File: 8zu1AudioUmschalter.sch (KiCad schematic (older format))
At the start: 39 parts, among them IC1 ATMEGA8A-A, IC2 MAX9890, J1 USB, J2 LUM 1503-07, J3 LUM 1503-07, J4 LUM 1503-07, J5 LUM 1503-07, J6 LUM 1503-07, J7 LUM 1503-07, J8 LUM 1503-07, J9 LUM 1503-07, K1 RELAY_2RT, K2 RELAY_2RT, K3 RELAY_2RT, K4 RELAY_2RT, K5 RELAY_2RT, K6 RELAY_2RT, K7 RELAY_2RT, U1 FT232RL, U2 ULN2003, Y1 16Mhz

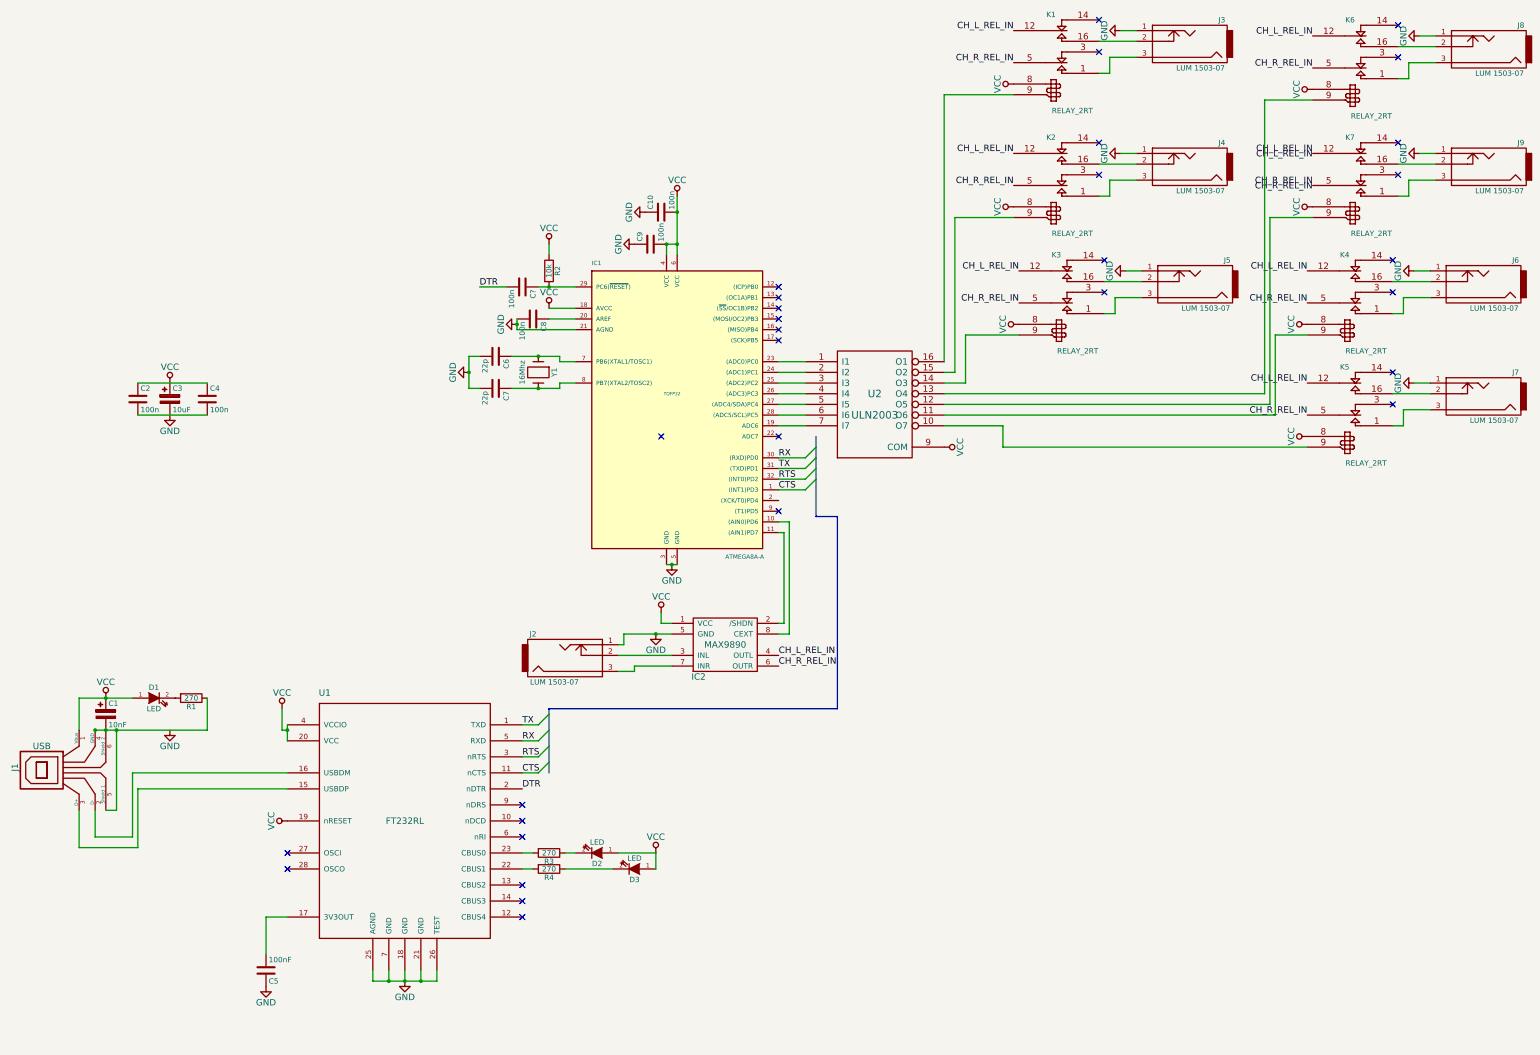
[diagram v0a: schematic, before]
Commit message: Kleinere Anpassungen am MAX9890
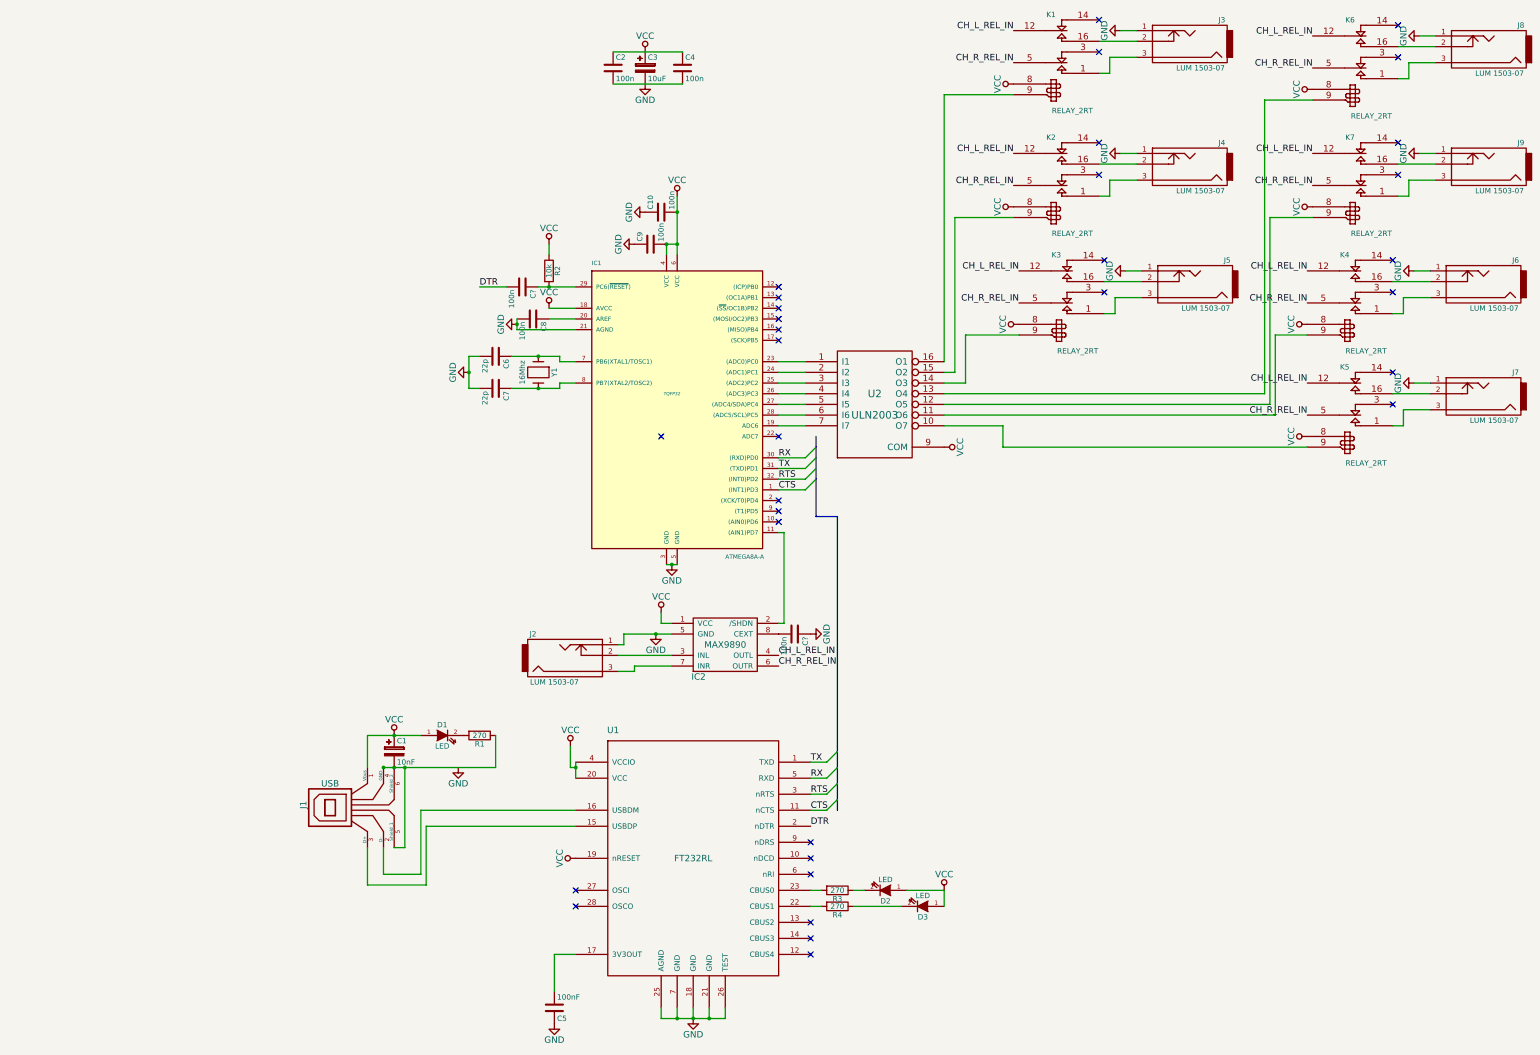
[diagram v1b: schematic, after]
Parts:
- added C?: 100n, symbol C
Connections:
- net GND: now also C?.1
- net at IC1.10 ((AIN0)PD6): no longer IC2.8 (CEXT)
- new net: C?.2, IC2.8 (CEXT)
- no-connect marks 31 -> 33
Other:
- moved on the sheet: C1, C2, C3, C4, C5, D1, D2, D3, J1, R1, R3, R4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

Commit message: Hinzufügen von Status LEDs für die einzelnen Relais
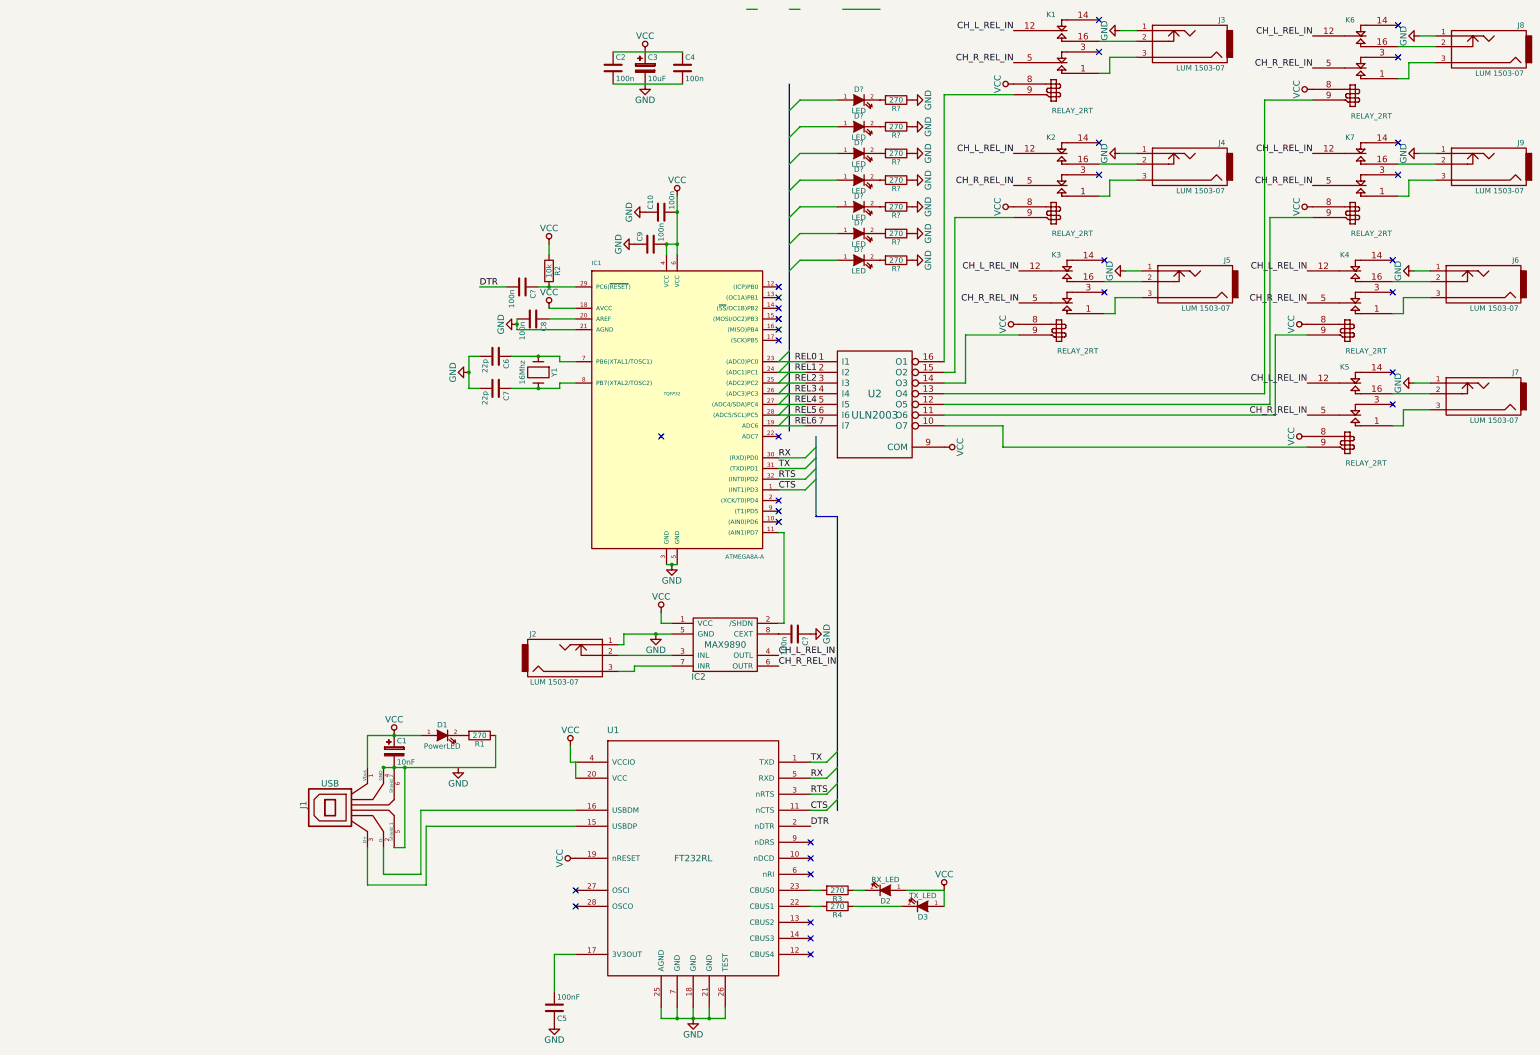
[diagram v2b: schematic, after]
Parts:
- added D? (x7): LED, symbol LED
- added R? (x7): 270, symbol R
- D1: value LED -> PowerLED
- D2: value LED -> RX_LED
- D3: value LED -> TX_LED
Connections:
- net labels added: REL0, REL1, REL2, REL3, REL4, REL5, REL6
- wire segments 151 -> 145

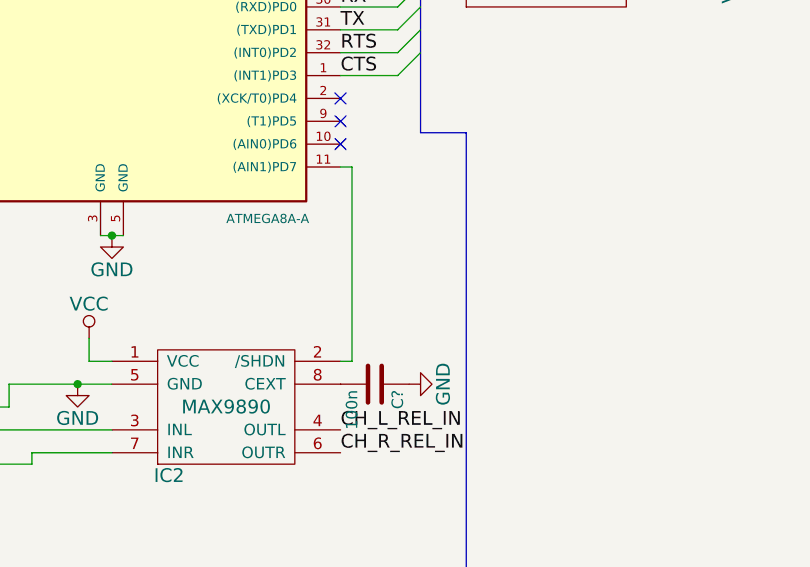
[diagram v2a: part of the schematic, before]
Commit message: Pull Down am MAX9890 um Signal bewusst zu kontrollieren
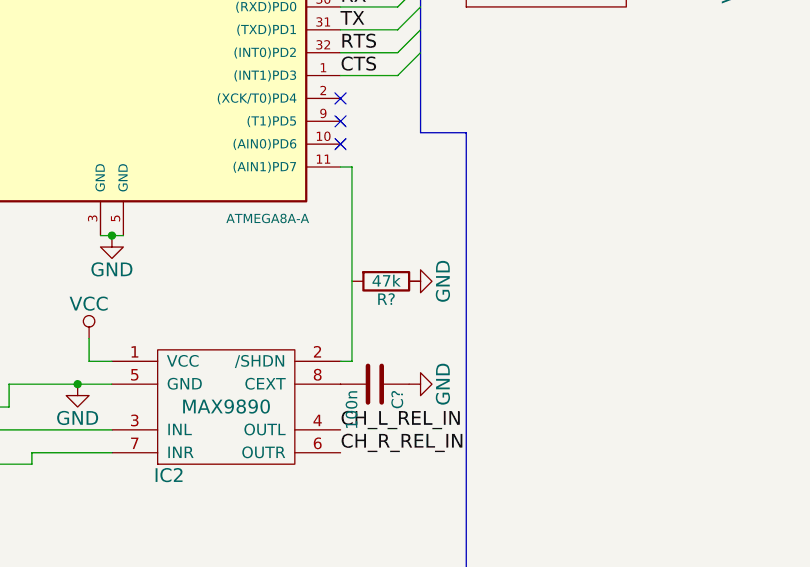
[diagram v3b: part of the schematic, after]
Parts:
- added R?: 47k, symbol R
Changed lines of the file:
@@
 Entry Wire Line
 	8350 3450 8450 3350
+$Comp
+L R R?
+U 1 1 5506D344
+P 8450 6400
+F 0 "R?" V 8530 6400 50  0000 C CNN
+F 1 "47k" V 8450 6400 50  0000 C CNN
+F 2 "" V 8380 6400 30  0000 C CNN
+F 3 "" H 8450 6400 30  0000 C CNN
+	1    8450 6400
+	0    1    1    0
+$EndComp
+$Comp
+L GND #PWR?
+U 1 1 5506D5D9
+P 8550 6400
+F 0 "#PWR?" H 8550 6150 60  0001 C CNN
+F 1 "GND" H 8550 6250 60  0000 C CNN
+F 2 "" H 8550 6400 60  0000 C CNN
+F 3 "" H 8550 6400 60  0000 C CNN
+	1    8550 6400
+	0    -1   -1   0
+$EndComp
 $EndSCHEMATC

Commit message: Hinzufügen der Libs
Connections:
- wire segments 145 -> 142
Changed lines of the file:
@@
 	0    1    1    0
 $EndComp
-Wire Wire Line
-	8350 1000 8450 1000
-Wire Wire Line
-	8050 1000 7950 1000
-Wire Wire Line
-	8850 1000 9200 1000
 $Comp
 L GND #PWR?

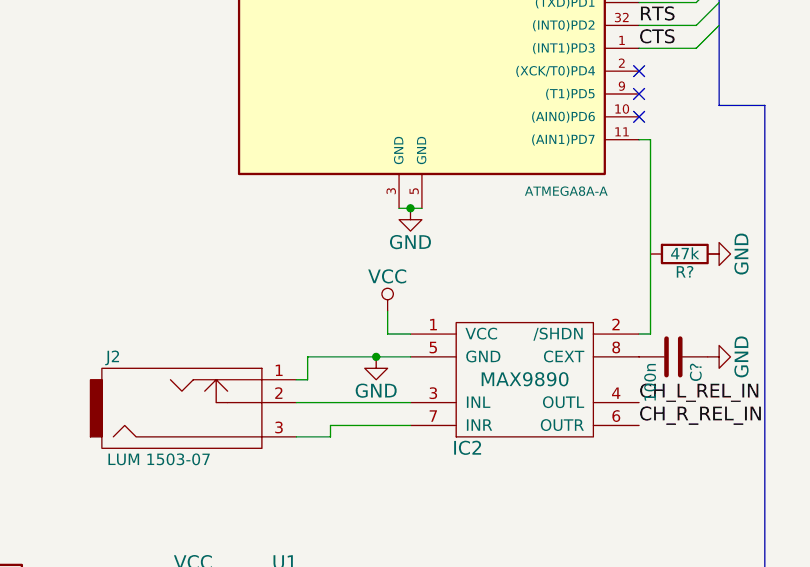
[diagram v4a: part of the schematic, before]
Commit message: Hinzufügen eines VCC stab. Kond. am MAX9890
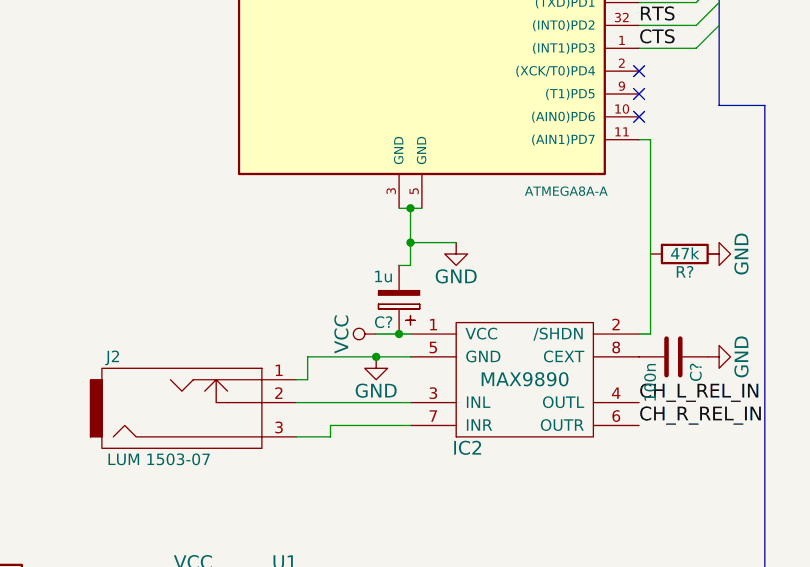
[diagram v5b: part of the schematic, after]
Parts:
- added C?: 1u, symbol CP
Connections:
- net GND: now also C?.2
- net VCC: now also C?.1
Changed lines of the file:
@@
 L GND #PWR017
 U 1 1 5504FEE4
-P 7250 6200
-F 0 "#PWR017" H 7250 5950 60  0001 C CNN
-F 1 "GND" H 7250 6050 60  0000 C CNN
-F 2 "" H 7250 6200 60  0000 C CNN
-F 3 "" H 7250 6200 60  0000 C CNN
-	1    7250 6200
+P 7450 6350
+F 0 "#PWR017" H 7450 6100 60  0001 C CNN
+F 1 "GND" H 7450 6200 60  0000 C CNN
+F 2 "" H 7450 6350 60  0000 C CNN
+F 3 "" H 7450 6350 60  0000 C CNN
+	1    7450 6350
 	1    0    0    -1
 $EndComp
@@
 Connection ~ 5350 4400
 Wire Wire Line
-	7250 6750 7150 6750
-Wire Wire Line
-	7150 6750 7150 6650
-Wire Wire Line
 	6800 6850 7250 6850
 $Comp
@@
 L VCC #PWR020
 U 1 1 55052107
-P 7150 6650
-F 0 "#PWR020" H 7150 6500 60  0001 C CNN
-F 1 "VCC" H 7150 6800 60  0000 C CNN
-F 2 "" H 7150 6650 60  0000 C CNN
-F 3 "" H 7150 6650 60  0000 C CNN
-	1    7150 6650
-	1    0    0    -1
+P 7100 6750
+F 0 "#PWR020" H 7100 6600 60  0001 C CNN
+F 1 "VCC" H 7100 6900 60  0000 C CNN
+F 2 "" H 7100 6750 60  0000 C CNN
+F 3 "" H 7100 6750 60  0000 C CNN
+	1    7100 6750
+	0    -1   -1   0
 $EndComp
 $Comp
@@
 	0    -1   -1   0
 $EndComp
+$Comp
+L CP C?
+U 1 1 5506F49A
+P 7200 6600
+F 0 "C?" H 7225 6700 50  0000 L CNN
+F 1 "1u" H 7225 6500 50  0000 L CNN
+F 2 "" H 7238 6450 30  0000 C CNN
+F 3 "" H 7200 6600 60  0000 C CNN
+	1    7200 6600
+	-1   0    0    1
+$EndComp
+Wire Wire Line
+	7100 6750 7250 6750
+Connection ~ 7200 6750
+Wire Wire Line
+	7200 6450 7250 6450
+Wire Wire Line
+	7250 6450 7250 6200
+Wire Wire Line
+	7450 6350 7250 6350
+Connection ~ 7250 6350
 $EndSCHEMATC

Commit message: Kleinere Anpassungen
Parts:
- removed C1: 10nF, symbol CP
- removed C3: 10uF, symbol CP
- removed C?: 1u, symbol CP
- added C1, C8: 10u, symbol C
- added C11: 1u, symbol C
- gave numbers to parts that had none: 17
- renumbered C4 to C12, C6 to C2, C7 to C4, C8 to C5, C5 to C6, C2 to C7, D3 to D10, D2 to D9, R3 to R4, R4 to R5
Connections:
- net GND: now also C2.1, C4.1, C5.1, J1.4 (GND), J1.5 (Shield_1), J1.6 (Shield_2), R1.1, R3.1, C1.2, C11.1, C8.2; no longer C2.2, C4.2, C5.2
- net REL0: now also D2.1 (A)
- net REL1: now also D3.1 (A)
- net REL2: now also D4.1 (A)
- net REL3: now also D5.1 (A)
- net REL4: now also D6.1 (A)
- net REL5: now also D7.1 (A)
- net REL6: now also D8.1 (A), IC1.17 ((SCK)PB5); no longer IC1.19 (ADC6)
- net VCC: now also C1.1, C11.2, C8.1
- net at IC1.11 ((AIN1)PD7), IC2.2 (/SHDN): now also R3.2
- net at IC1.20 (AREF): now also C5.2; no longer C5.1
- net at IC1.7 (PB6(XTAL1/TOSC1)), Y1.1: now also C2.2; no longer C2.1
- net at IC1.8 (PB7(XTAL2/TOSC2)), Y1.2: now also C4.2; no longer C4.1
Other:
- moved on the sheet: C2, C4, C5, D1, J1, R1
